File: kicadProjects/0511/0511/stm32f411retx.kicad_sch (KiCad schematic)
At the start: 9 parts, among them U8 STM32F411RETx

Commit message: stm32 bloc implementation
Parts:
- added C? (x5): C, symbol Device:C
- added C?: C_Polarized, symbol Device:C_Polarized
- added R?: R, symbol Device:R
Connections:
- net +3.3V: now also JP4.1 (Pin_1)
- net GND: now also JP4.3 (Pin_3), JP5.3 (Pin_3), C?.1, C?.1, C?.1, C?.1, C?.1, C?.2, R?.2
- net USART_TX: now reaches U8.16 (PA2)
- net USART_TX: now also JP5.2 (Pin_2)
- net USART_RX: now reaches U8.17 (PA3)
- net USART_RX: now also JP5.1 (Pin_1)
- net at U8.30 (VCAP1): now also C?.1
- net SWO: now reaches U8.55 (PB3)
- net SWO: now also JP4.6 (Pin_6)
- net BOOT0: now reaches U8.60 (BOOT0)
- net BOOT0: now also R?.1
- net NRST: now reaches C?.1, SW?.1, U8.7 (NRST)
- net NRST: now also JP4.5 (Pin_5)
- net TCK: now reaches JP4.2 (Pin_2)
- net TMS: now reaches JP4.4 (Pin_4)
- new net: C?.2, C?.2, C?.2, C?.2, C?.2

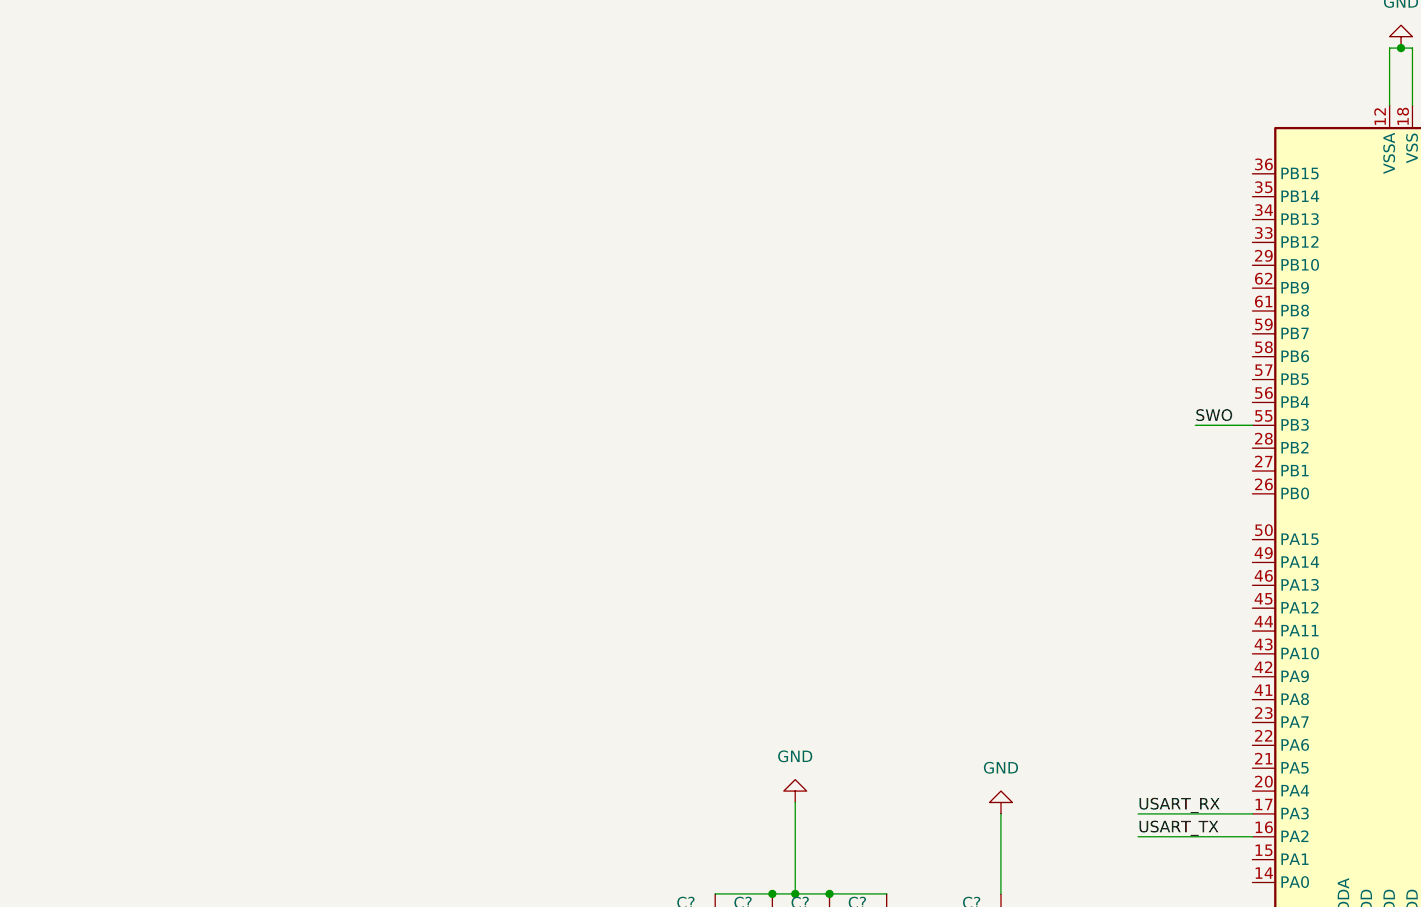
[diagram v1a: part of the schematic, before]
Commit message: started to add hierarchical pins
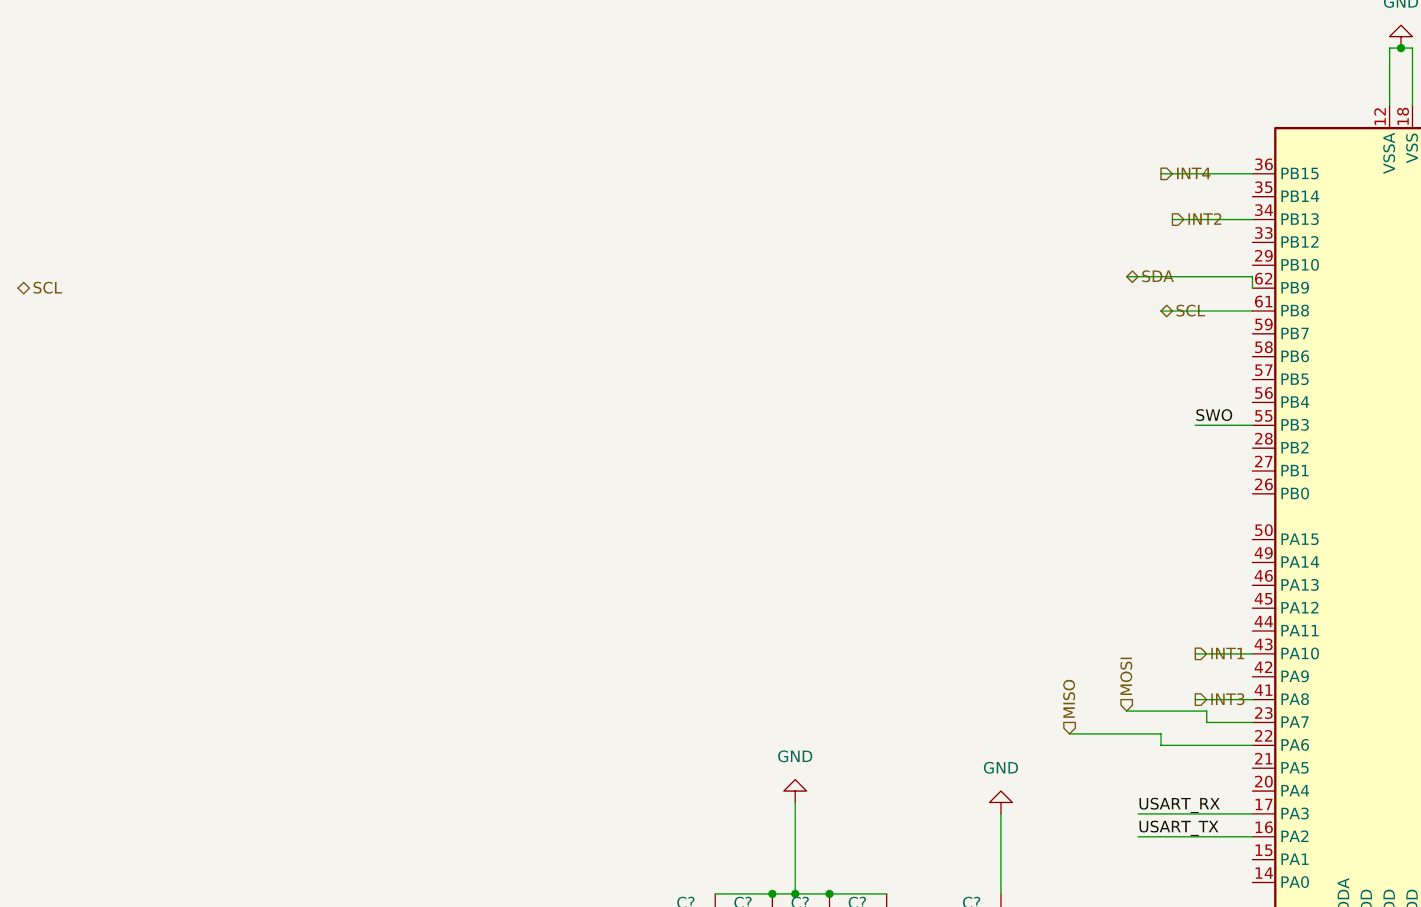
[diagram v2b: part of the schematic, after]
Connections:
- net MISO: now reaches U8.22 (PA6)
- net MOSI: now reaches U8.23 (PA7)
- net INT2: now reaches U8.34 (PB13)
- net INT4: now reaches U8.36 (PB15)
- net INT3: now reaches U8.41 (PA8)
- net INT1: now reaches U8.43 (PA10)
- net SCL: now reaches U8.61 (PB8)
- net SDA: now reaches U8.62 (PB9)
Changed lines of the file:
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@@
+	(wire
+		(pts
+			(xy 74.93 106.68) (xy 81.28 106.68)
+		)
+		(stroke
+			(width 0)
+			(type default)
+		)
+	)
+	(wire
+		(pts
+			(xy 60.96 110.49) (xy 71.12 110.49)
+		)
+		(stroke
+			(width 0)
+			(type default)
+		)
+	)
 	(wire
 		(pts
@@
 	(wire
 		(pts
+			(xy 74.93 101.6) (xy 81.28 101.6)
+		)
+		(stroke
+			(width 0)
+			(type default)
+		)
+	)
+	(wire
+		(pts
 			(xy 116.84 68.58) (xy 130.81 68.58)
 		)
@@
 	(wire
 		(pts
+			(xy 71.12 48.26) (xy 81.28 48.26)
+		)
+		(stroke
+			(width 0)
+			(type default)
+		)
+	)
+	(wire
+		(pts
 			(xy 91.44 144.78) (xy 83.82 144.78)
 		)
@@
 	(wire
 		(pts
+			(xy 76.2 109.22) (xy 81.28 109.22)
+		)
+		(stroke
+			(width 0)
+			(type default)
+		)
+	)
+	(wire
+		(pts
 			(xy 119.38 120.65) (xy 119.38 121.92)
 		)
@@
 	(wire
 		(pts
+			(xy 67.31 59.69) (xy 81.28 59.69)
+		)
+		(stroke
+			(width 0)
+			(type default)
+		)
+	)
+	(wire
+		(pts
 			(xy 93.98 134.62) (xy 93.98 144.78)
 		)
@@
 	(wire
 		(pts
+			(xy 71.12 110.49) (xy 71.12 111.76)
+		)
+		(stroke
+			(width 0)
+			(type default)
+		)
+	)
+	(wire
+		(pts
 			(xy 30.48 128.27) (xy 34.29 128.27)
 		)
@@
 	(wire
 		(pts
+			(xy 72.39 53.34) (xy 81.28 53.34)
+		)
+		(stroke
+			(width 0)
+			(type default)
+		)
+	)
+	(wire
+		(pts
 			(xy 133.35 127) (xy 121.92 127)
 		)
@@
 	(wire
 		(pts
+			(xy 67.31 107.95) (xy 76.2 107.95)
+		)
+		(stroke
+			(width 0)
+			(type default)
+		)
+	)
+	(wire
+		(pts
 			(xy 96.52 34.29) (xy 97.79 34.29)
 		)
@@
 	(wire
 		(pts
+			(xy 76.2 107.95) (xy 76.2 109.22)
+		)
+		(stroke
+			(width 0)
+			(type default)
+		)
+	)
+	(wire
+		(pts
 			(xy 27.94 135.89) (xy 34.29 135.89)
 		)
@@
 	(wire
 		(pts
+			(xy 81.28 59.69) (xy 81.28 60.96)
+		)
+		(stroke
+			(width 0)
+			(type default)
+		)
+	)
+	(wire
+		(pts
 			(xy 133.35 137.16) (xy 133.35 147.32)
 		)
@@
 	(wire
 		(pts
+			(xy 71.12 63.5) (xy 81.28 63.5)
+		)
+		(stroke
+			(width 0)
+			(type default)
+		)
+	)
+	(wire
+		(pts
 			(xy 196.85 86.36) (xy 196.85 85.09)
 		)
@@
 		(pts
 			(xy 130.81 68.58) (xy 130.81 71.12)
+		)
+		(stroke
+			(width 0)
+			(type default)
+		)
+	)
+	(wire
+		(pts
+			(xy 71.12 111.76) (xy 81.28 111.76)
 		)
 		(stroke
@@
 		)
 	)
+	(hierarchical_label "INT4"
+		(shape output)
+		(at 71.12 48.26 0)
+		(effects
+			(font
+				(size 1.27 1.27)
+			)
+			(justify left)
+		)
+	)
+	(hierarchical_label "INT2"
+		(shape output)
+		(at 72.39 53.34 0)
+		(effects
+			(font
+				(size 1.27 1.27)
+			)
+			(justify left)
+		)
+	)
+	(hierarchical_label "SDA"
+		(shape bidirectional)
+		(at 67.31 59.69 0)
+		(effects
+			(font
+				(size 1.27 1.27)
+			)
+			(justify left)
+		)
+	)
+	(hierarchical_label "MOSI"
+		(shape input)
+		(at 67.31 107.95 90)
+		(effects
+			(font
+				(size 1.27 1.27)
+			)
+			(justify left)
+		)
+	)
+	(hierarchical_label "SCL"
+		(shape bidirectional)
+		(at -55.88 60.96 0)
+		(effects
+			(font
+				(size 1.27 1.27)
+			)
+			(justify left)
+		)
+	)
+	(hierarchical_label "MISO"
+		(shape input)
+		(at 60.96 110.49 90)
+		(effects
+			(font
+				(size 1.27 1.27)
+			)
+			(justify left)
+		)
+	)
+	(hierarchical_label "INT3"
+		(shape output)
+		(at 74.93 106.68 0)
+		(effects
+			(font
+				(size 1.27 1.27)
+			)
+			(justify left)
+		)
+	)
+	(hierarchical_label "INT1"
+		(shape output)
+		(at 74.93 101.6 0)
+		(effects
+			(font
+				(size 1.27 1.27)
+			)
+			(justify left)
+		)
+	)
+	(hierarchical_label "SCL"
+		(shape bidirectional)
+		(at 71.12 63.5 0)
+		(effects
+			(font
+				(size 1.27 1.27)
+			)
+			(justify left)
+		)
+	)

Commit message: poursuite
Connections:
- net WSEL: now reaches U8.20 (PA4)
- net BCLCK: now reaches U8.21 (PA5)
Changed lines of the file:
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@@
+	(wire
+		(pts
+			(xy 73.66 116.84) (xy 81.28 116.84)
+		)
+		(stroke
+			(width 0)
+			(type default)
+		)
+	)
 	(wire
 		(pts
@@
 		(pts
 			(xy 104.14 138.43) (xy 104.14 140.97)
+		)
+		(stroke
+			(width 0)
+			(type default)
+		)
+	)
+	(wire
+		(pts
+			(xy 68.58 114.3) (xy 81.28 114.3)
 		)
 		(stroke
@@
 		)
 	)
+	(hierarchical_label "WSEL"
+		(shape bidirectional)
+		(at 73.66 116.84 0)
+		(effects
+			(font
+				(size 1.27 1.27)
+			)
+			(justify left)
+		)
+	)
 	(hierarchical_label "INT2"
 		(shape output)
@@
 		(effects
 			(font
+				(size 1.27 1.27)
+			)
+			(justify left)
+		)
+	)
+	(hierarchical_label "BCLCK"
+		(shape bidirectional)
+		(at 68.58 114.3 0)
+		(effects
+			(font

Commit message: assignation empreintes
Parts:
- C74: renamed from C?; footprint (none) -> Capacitor_Tantalum_SMD:CP_EIA-6032-28_Kemet-C
- C75, C76, C77, C78, C79, C80, C81, C82, C83: renamed from C?; footprint (none) -> Capacitor_SMD:C_0603_1608Metric
- JP1: renamed from JP4; footprint (none) -> Connector_PinSocket_2.54mm:PinSocket_1x06_P2.54mm_Vertical
- JP2: renamed from JP5; footprint (none) -> Connector_PinSocket_2.54mm:PinSocket_1x03_P2.54mm_Vertical
- R154: renamed from R?; footprint (none) -> Resistor_SMD:R_0603_1608Metric
- SW68: renamed from SW?; footprint (none) -> Button_Switch_Keyboard:SW_Cherry_MX_1.00u_PCB
- Y1: renamed from Y?; footprint (none) -> Crystal:Crystal_SMD_3215-2Pin_3.2x1.5mm
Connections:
- net FSR: now reaches U8.15 (PA1)

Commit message: added comments
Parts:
- added J1: USB_B, Connector_USB:USB_Micro-B_Molex_47346-0001, symbol Connector:USB_B
- added R154: 10K, Resistor_SMD:R_0603_1608Metric, symbol Device:R
- added R155: 20K, Resistor_SMD:R_0603_1608Metric, symbol Device:R
- added R156: 1.5K, Resistor_SMD:R_0603_1608Metric, symbol Device:R
- renumbered R154 to R157
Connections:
- net TCK is gone; now on net SWCLK: JP1.2 (Pin_2)
- net TMS is gone; now on net SWDIO: JP1.4 (Pin_4)
- net +3.3V: now also C77.2, C78.2, C79.2, C80.2, C81.2, R156.1
- net GND: now also J1.4 (GND), R155.2
- net at C75.2, Y1.2: now also U8.6 (PH1); no longer U8.4 (PC15)
- net at C76.1, Y1.1: now also U8.5 (PH0); no longer U8.3 (PC14)
- net IS_USB_PLUGGED: now reaches U8.42 (PA9)
- net IS_USB_PLUGGED: now also R154.2, R155.1
- net at U8.44 (PA11): now also J1.2 (D-)
- net at U8.45 (PA12): now also J1.3 (D+), R156.2
- net SWDIO: now reaches U8.46 (PA13)
- net SWCLK: now reaches U8.49 (PA14)
- new net VBUS: J1.1 (VBUS), R154.1
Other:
- note added: "- J'ai momdifié la position du quartz pour avoir une horloge rapide nécessaire au midi. - Il y a un diviseur de tension maintenant pour lire la valeur de VBUS quand ln branche en usb afin de transformer le 5v en 3v environ. (ce sera utilisé pour voir si on active le mode midi lors du branchement usb) - J'ai modifié les nommages des pins de débug mais normalement ça reste comme sur ton schema - j'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"
- moved on the sheet: C75, C76, Y1

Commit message: add values
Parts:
- C75, C76: value C -> 22pF
- C82: value C -> 0.1uF
- Y1: value Crystal -> 8MHz
- renumbered C74 to 4.7uF
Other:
- moved on the sheet: R156
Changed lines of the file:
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@@
 	(wire
 		(pts
-			(xy 54.61 80.01) (xy 54.61 86.36)
+			(xy 54.61 80.01) (xy 54.61 82.55)
 		)
 		(stroke
@@
 	(wire
 		(pts
-			(xy 54.61 93.98) (xy 54.61 96.52)
+			(xy 54.61 90.17) (xy 54.61 96.52)
 		)
 		(stroke
@@
 			)
 		)
-		(property "Value" "C"
+		(property "Value" "22pF"
 			(at 161.798 98.044 90)
 			(effects
@@
 			)
 		)
-		(property "Value" "Crystal"
+		(property "Value" "8MHz"
 			(at 151.13 111.7599 90)
 			(effects
@@
 	(symbol
 		(lib_id "Device:R")
-		(at 54.61 90.17 0)
+		(at 54.61 86.36 0)
 		(unit 1)
 		(exclude_from_sim no)
@@
 		(fields_autoplaced yes)
 		(property "Reference" "R156"
-			(at 57.15 88.8999 0)
+			(at 57.15 85.0899 0)
 			(effects
 				(font
@@
 		)
 		(property "Value" "1.5K"
-			(at 57.15 91.4399 0)
+			(at 57.15 87.6299 0)
 			(effects
 				(font
@@
 		)
 		(property "Footprint" "Resistor_SMD:R_0603_1608Metric"
-			(at 52.832 90.17 90)
+			(at 52.832 86.36 90)
 			(effects
 				(font
@@
 		)
 		(property "Datasheet" "~"
-			(at 54.61 90.17 0)
+			(at 54.61 86.36 0)
 			(effects
 				(font
@@
 		)
 		(property "Description" "Resistor"
-			(at 54.61 90.17 0)
+			(at 54.61 86.36 0)
 			(effects
 				(font
@@
 		(dnp no)
 		(fields_autoplaced yes)
-		(property "Reference" "C74"
+		(property "Reference" "4.7uF"
 			(at 122.301 49.53 90)
 			(effects
@@
 			(project ""
 				(path "/2c0b0e0d-c5e7-48b7-93bb-9be1941509af/7f025c79-ea20-4013-a71e-871359ae3c80"
-					(reference "C74")
+					(reference "4.7uF")
 					(unit 1)
 				)
@@
 			)
 		)
-		(property "Value" "C"
+		(property "Value" "0.1uF"
 			(at 127.254 135.382 0)
 			(effects
@@
 			)
 		)
-		(property "Value" "C"
+		(property "Value" "22pF"
 			(at 165.862 124.206 90)
 			(effects

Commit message: imported compoents
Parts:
- removed J1: USB_B, Connector_USB:USB_Micro-B_Molex_47346-0001, symbol Connector:USB_B
- removed R156: 1.5K, Resistor_SMD:R_0603_1608Metric, symbol Device:R
- added C72, C73: 4.3pF, Capacitor_SMD:C_0603_1608Metric, symbol Device:C
- added C?: ~, Capacitor_SMD:C_0603_1608Metric, symbol Device:C
- added D?: ESD9L5.0ST5G, ESD9L5.0ST5G:DIOM1006X40N, symbol ABS25-32.768KHZ-6-T:ESD9L5.0ST5G
- added J?: USB4120-03-C_REVA6, USB4120-03-C_REVA6:GCT_USB4120-03-C_REVA6, symbol ABS25-32.768KHZ-6-T:USB4120-03-C_REVA6
- added R?: ~, Resistor_SMD:R_0603_1608Metric, symbol Device:R
- added R?: 1.5K, Resistor_SMD:R_0603_1608Metric, symbol Device:R
- added Y?: 32.768KHz, ABS25-32.768KHZ-6-T:XTAL_ABS25-32.768KHZ-6-T, symbol ABS25-32.768KHZ-6-T:ABS25-32.768KHZ-6-T
- C76: renamed from C77; value C -> 0.1uF
- C77: renamed from C78; value C -> 0.1uF
- C78: renamed from C79; value C -> 0.1uF
- C79: renamed from C80; value C -> 0.1uF
- C80: renamed from C81; value C -> 0.1uF
- renumbered 4.7uF to 4.7uF1, C75 to C74, C76 to C75, C82 to C81, C83 to C82, R154 to R151, R155 to R152, R157 to R154, U8 to U6, Y1 to Y2
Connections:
- net +3.3V: now also R?.1
- net GND: now also C72.1, C73.2, C?.2, J?.A1 (GND_A), J?.A12 (GND_A), J?.B1 (GND_B), J?.B12 (GND_B), R?.2
- net at U6.3 (PC14): now also C73.1, Y?.1
- net at U6.4 (PC15): now also C72.2, Y?.4
- net PA11: now reaches U6.44 (PA11)
- net PA11: now also J?.A7 (D1-), J?.B7 (D2-)
- net D1+: now reaches U6.45 (PA12)
- net D1+: now also J?.A6 (D1+), J?.B6 (D2+), R?.2
- new net: C?.1, J?.S1 (SHIELD), J?.S2 (SHIELD), J?.S3 (SHIELD), J?.S4 (SHIELD), R?.1
- new net VBUS_A: J?.A4 (VBUS_A), J?.A9 (VBUS_A)
- new net VBUS_B: J?.B4 (VBUS_B), J?.B9 (VBUS_B)
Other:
- note added: "A REMPLACER DIVISEUR PAR LDO"
- note added: "METTRE FERRITE POUR FILTRER HAUTES FREQUENCES VDDA"
- note added: "mettre un LDO p(régulateur de tension linéraire) our transformer le 5v en 3.3v changer le bloc en usbc et ajouter shield choisir LDO : https://www.digikey.fr/fr/products/filter/r%C3%A9gulateurs-de-tension-r%C3%A9gulateurs-lin%C3%A9aires-%C3%A0-faible-chute-de-tension-ldo/699 mettre oscillateur avec quartz voir ref"

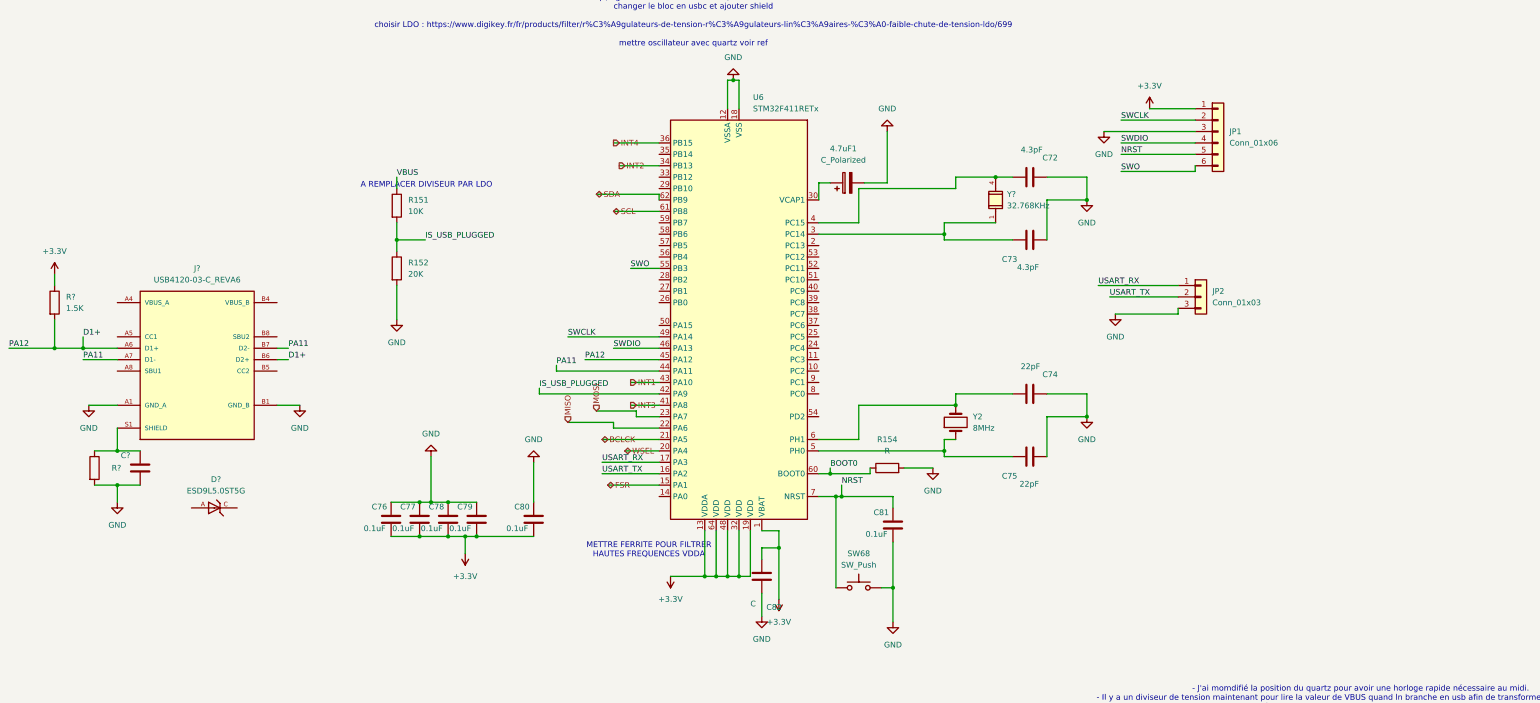
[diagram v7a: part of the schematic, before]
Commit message: added LDO, quartz, usb c
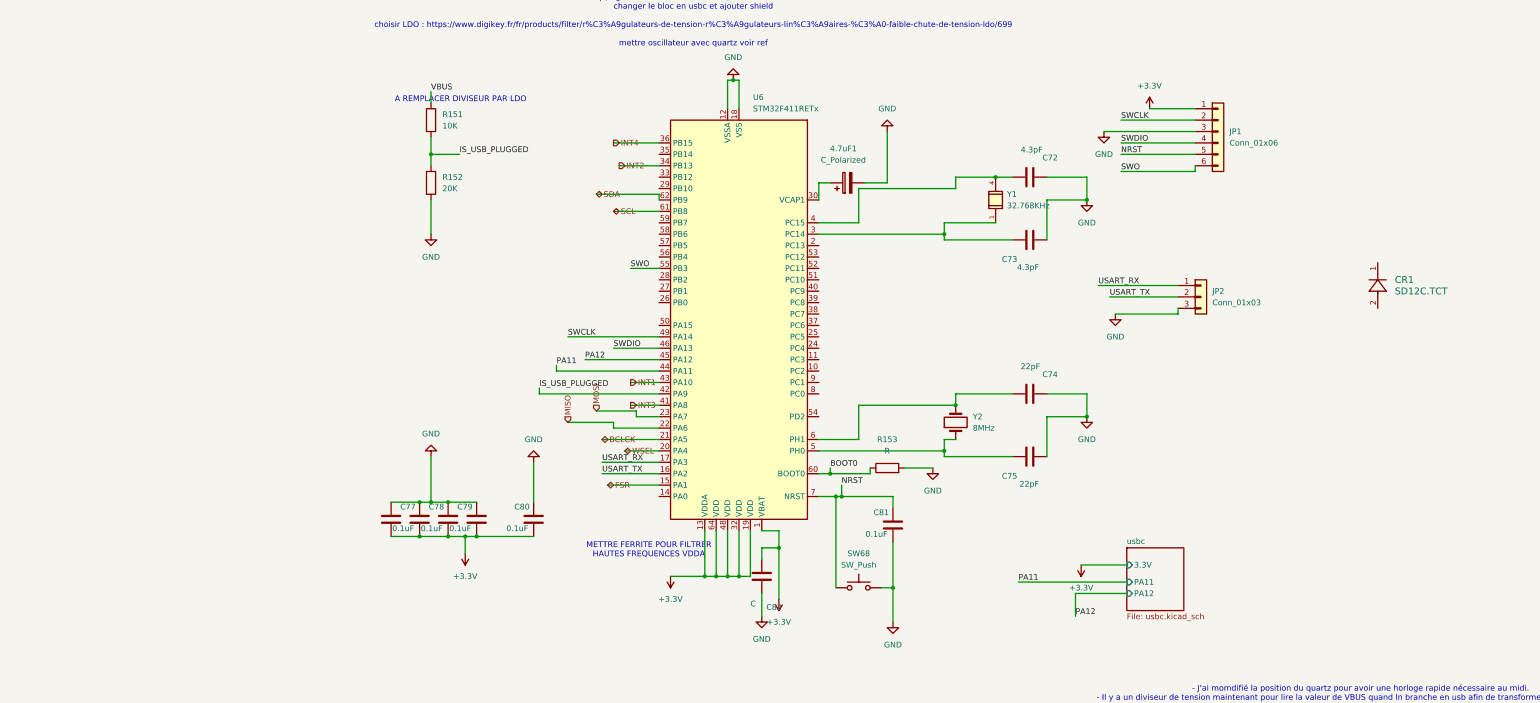
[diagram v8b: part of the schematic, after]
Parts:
- removed C?: ~, Capacitor_SMD:C_0603_1608Metric, symbol Device:C
- removed D?: ESD9L5.0ST5G, ESD9L5.0ST5G:DIOM1006X40N, symbol ABS25-32.768KHZ-6-T:ESD9L5.0ST5G
- removed J?: USB4120-03-C_REVA6, USB4120-03-C_REVA6:GCT_USB4120-03-C_REVA6, symbol ABS25-32.768KHZ-6-T:USB4120-03-C_REVA6
- removed R?: ~, Resistor_SMD:R_0603_1608Metric, symbol Device:R
- removed R?: 1.5K, Resistor_SMD:R_0603_1608Metric, symbol Device:R
- added CR1: SD12C.TCT, Project:CR_SD05_SEM, symbol ABS25-32.768KHZ-6-T:SD12C.TCT
- Y1: renamed from Y?; footprint ABS25-32.768KHZ-6-T:XTAL_ABS25-32.768KHZ-6-T -> Project:XTAL_ABS25-32.768KHZ-6-T
- renumbered R154 to R153
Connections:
- net D1+ renamed PA12
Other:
- added sheet usbc (usbc.kicad_sch)
- moved on the sheet: R151, R152
